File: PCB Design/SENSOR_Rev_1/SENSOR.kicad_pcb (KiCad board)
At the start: 2 copper layers, 40 x 65 mm, 17 parts, among them J1 Conn_01x24_Pin, J2 Conn_01x24_Pin, U1 MS583730BA01-50, U2 LIS2HH12TR, U3 MMC5603NJ, U4 LSM6DSO32TR

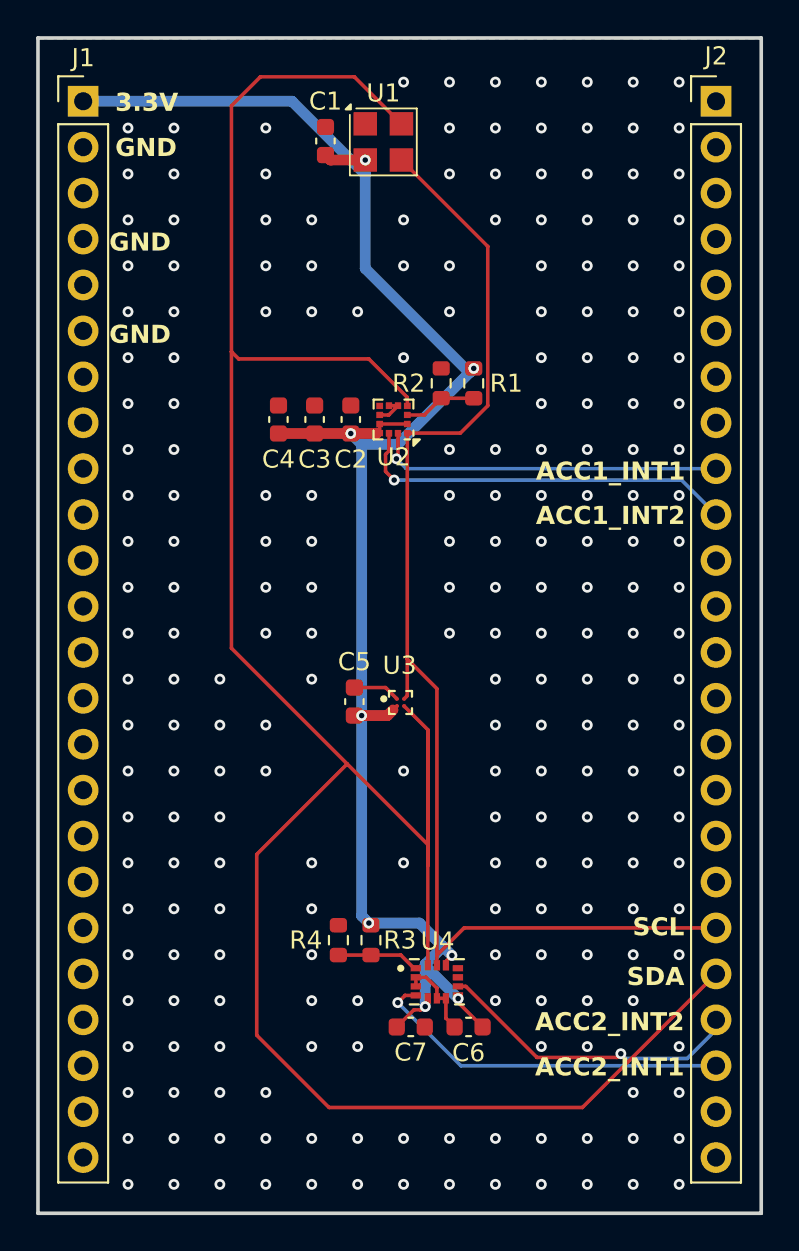
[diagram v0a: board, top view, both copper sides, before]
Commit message: Added Sensor Names to Silkscreen
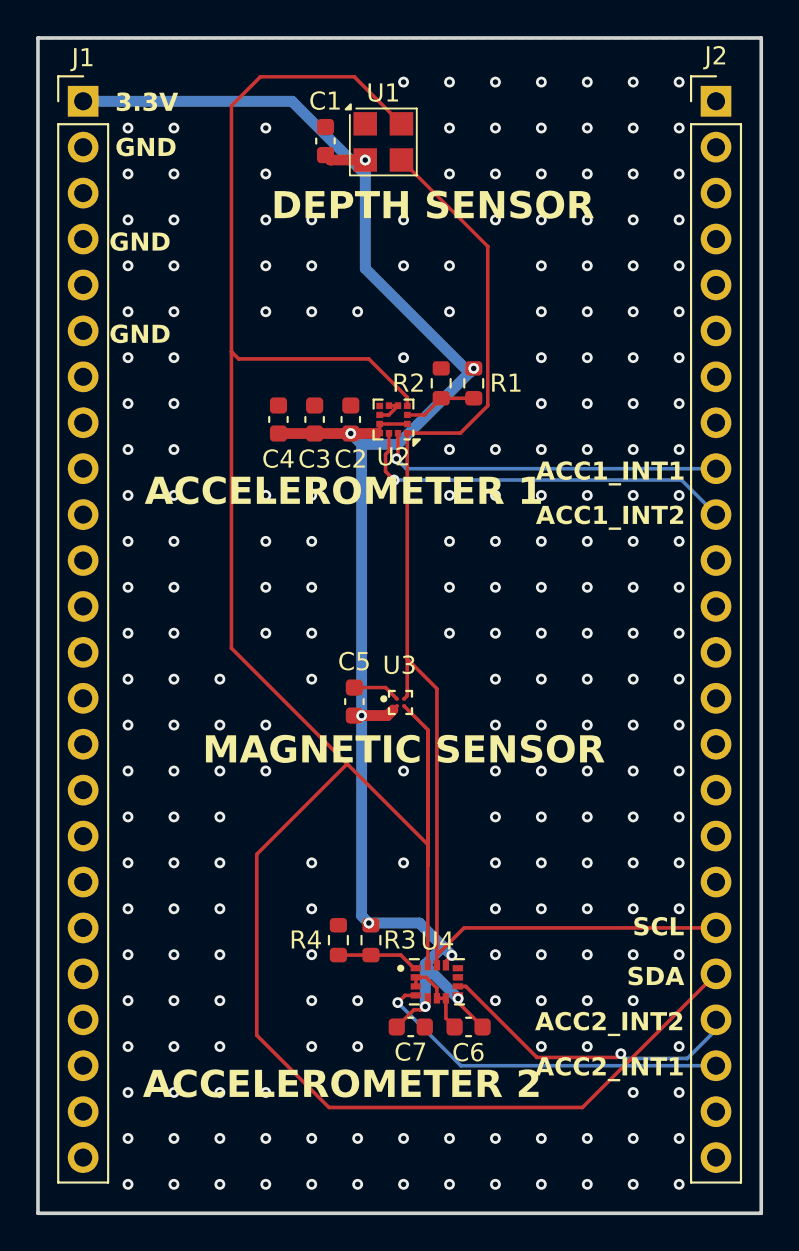
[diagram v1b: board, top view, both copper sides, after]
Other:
- board text added: "ACCELEROMETER 1"
- board text added: "ACCELEROMETER 2"
- board text added: "DEPTH SENSOR"
- board text added: "MAGNETIC SENSOR"
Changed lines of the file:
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@@
 			(drillshape 0)
 			(scaleselection 1)
-			(outputdirectory "SENSOR_BOARD_OUTPUT_08_18_2026/")
+			(outputdirectory "SENSOR_BOARD_OUTPUT_08_19_2026/")
 		)
 	)
@@
 		)
 	)
+	(gr_text "ACCELEROMETER 1"
+		(at 138.4 91.2 0)
+		(layer "F.SilkS")
+		(effects
+			(font
+				(size 1.5 1.5)
+				(thickness 0.3)
+				(bold yes)
+			)
+			(justify left bottom)
+		)
+	)
+	(gr_text "ACCELEROMETER 2"
+		(at 138.3 124 0)
+		(layer "F.SilkS")
+		(effects
+			(font
+				(size 1.5 1.5)
+				(thickness 0.3)
+				(bold yes)
+			)
+			(justify left bottom)
+		)
+	)
 	(gr_text "3.3V"
 		(at 136.76881 69.4 0)
@@
 		)
 	)
+	(gr_text "DEPTH SENSOR"
+		(at 145.4 75.4 0)
+		(layer "F.SilkS")
+		(effects
+			(font
+				(size 1.5 1.5)
+				(thickness 0.3)
+				(bold yes)
+			)
+			(justify left bottom)
+		)
+	)
 	(gr_text "SCL"
 		(at 168.25 115 0)
@@
 		)
 	)
+	(gr_text "MAGNETIC SENSOR"
+		(at 141.6 105.5 0)
+		(layer "F.SilkS")
+		(effects
+			(font
+				(size 1.5 1.5)
+				(thickness 0.3)
+				(bold yes)
+			)
+			(justify left bottom)
+		)
+	)

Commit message: Updated Sensor to new Version
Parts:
- U2: value LIS2HH12TR -> ASM330LHHXG1TR; footprint Package_LGA:LGA-12_2x2mm_P0.5mm -> SENSOR:LGA14_2P5X3_STM
- moved C3 2.60 mm to (149.1, 88.6), turned to 180 degrees
- moved C4 2.40 mm to (148.2, 86.2), turned to -90 degrees
- moved U2 0.29 mm to (152.3, 86.6), turned to -90 degrees
- moved C2 0.15 mm to (149.8, 86.2), turned to -90 degrees
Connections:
- U2 pad 1: /SCL -> /ACC1_ADD
- U2 pad 10: 3.3V -> unconnected-(U2-NC-Pad10)
- U2 pad 11: /ACC1_INT2 -> unconnected-(U2-NC-Pad11)
- U2 pad 12: /ACC1_INT1 -> 3.3V
- U2 pad 3: /ACC1_ADD -> 3.3V
- U2 pad 4: /SDA -> /ACC1_INT1
- U2 pad 5: GND -> 3.3V
- U2 pad 6: GND -> unconnected-(U2-NC-Pad6)
- U2 pad 8: GND -> 3.3V
- U2 pad 9: 3.3V -> /ACC1_INT2
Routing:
- net 3.3V: track 97.6 -> 105.3 mm, vias 8 -> 9
- net /ACC1_INT1: track 19.4 -> 21.2 mm
- net /SDA: track 138.4 -> 140.3 mm, vias 0 -> 2
- net /SCL: track 69.1 -> 70.8 mm
- net GND: track 9.07 -> 10.6 mm, vias 229 -> 232
- net /ACC1_INT2: track 21.5 -> 20.0 mm

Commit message: Claude PCB Review
Made updates based on Claude's Review
- Added decoupling capacitor
- Verified CS pins
- Compared placement and connections to data sheets
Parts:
- added C8: 10u, Capacitor_SMD:C_0603_1608Metric, F.Cu at (153.1, 121.5)
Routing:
- net 3.3V: track 105.3 -> 106.9 mm
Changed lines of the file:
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@@
 			(net 32 "/ACC1_ADD")
 			(pinfunction "SDO/SA0")
-			(pintype "unspecified")
+			(pintype "passive")
 		)
 		(pad "2" smd rect
@@
 			(net 1 "3.3V")
 			(pinfunction "MSDA")
-			(pintype "unspecified")
+			(pintype "passive")
 		)
 		(pad "3" smd rect
@@
 			(net 1 "3.3V")
 			(pinfunction "MSCL")
-			(pintype "unspecified")
+			(pintype "passive")
 		)
 		(pad "4" smd rect
@@
 			(net 35 "/ACC1_INT1")
 			(pinfunction "INT1")
-			(pintype "unspecified")
+			(pintype "passive")
 		)
 		(pad "5" smd rect
@@
 			(net 34 "/ACC1_INT2")
 			(pinfunction "INT2")
-			(pintype "unspecified")
+			(pintype "passive")
 		)
 		(pad "10" smd rect
@@
 			(net 1 "3.3V")
 			(pinfunction "CS")
-			(pintype "unspecified")
+			(pintype "passive")
 		)
 		(pad "13" smd rect
@@
 			(net 3 "/SCL")
 			(pinfunction "SCL")
-			(pintype "unspecified")
+			(pintype "passive")
 		)
 		(pad "14" smd rect
@@
 			(net 2 "/SDA")
 			(pinfunction "SDA")
-			(pintype "unspecified")
+			(pintype "passive")
 		)
 		(embedded_fonts no)
@@
 		(tags "capacitor")
 		(property "Reference" "C7"
-			(at 0 1.4 0)
+			(at -2.515 0.055 0)
 			(layer "F.SilkS")
 			(effects
@@
 		)
 	)
+	(footprint "Capacitor_SMD:C_0603_1608Metric"
+		(layer "F.Cu")
+		(at 153.125 121.5)
+		(descr "Capacitor SMD 0603 (1608 Metric), square (rectangular) end terminal, IPC-7351 nominal, (Body size source: IPC-SM-782 page 76, https://www.pcb-3d.com/wordpress/wp-content/uploads/ipc-sm-782a_amendment_1_and_2.pdf), generated with kicad-footprint-generator")
+		(tags "capacitor")
+		(property "Reference" "C8"
+			(at -2.425 0.1 0)
+			(layer "F.SilkS")
+			(effects
+				(font
+					(size 1 1)
+					(thickness 0.15)
+				)
+			)
+		)
+		(property "Value" "10u"
+			(at 0 1.43 0)
+			(layer "F.Fab")
+			(effects
+				(font
+					(size 1 1)
+					(thickness 0.15)
+				)
+			)
+		)
+		(property "Datasheet" "~"
+			(at 0 0 0)
+			(layer "F.Fab")
+			(hide yes)
+			(effects
+				(font
+					(size 1.27 1.27)
+					(thickness 0.15)
+				)
+			)
+		)
+		(property "Description" "Unpolarized capacitor"
+			(at 0 0 0)
+			(layer "F.Fab")
+			(hide yes)
+			(effects
+				(font
+					(size 1.27 1.27)
+					(thickness 0.15)
+				)
+			)
+		)
+		(property ki_fp_filters "C_*")
+		(sheetname "/")
+		(sheetfile "SENSOR.kicad_sch")
+		(attr smd)
+		(fp_line
+			(start -0.14058 -0.51)
+			(end 0.14058 -0.51)
+			(stroke
+				(width 0.12)
+				(type solid)
+			)
+			(layer "F.SilkS")
+		)
+		(fp_line
+			(start -0.14058 0.51)
+			(end 0.14058 0.51)
+			(stroke
+				(width 0.12)
+				(type solid)
+			)
+			(layer "F.SilkS")
+		)
+		(fp_line
+			(start -1.48 -0.73)
+			(end 1.48 -0.73)
+			(stroke
+				(width 0.05)
+				(type solid)
+			)
+			(layer "F.CrtYd")
+		)
+		(fp_line
+			(start -1.48 0.73)
+			(end -1.48 -0.73)
+			(stroke
+				(width 0.05)
+				(type solid)
+			)
+			(layer "F.CrtYd")
+		)
+		(fp_line
+			(start 1.48 -0.73)
+			(end 1.48 0.73)
+			(stroke
+				(width 0.05)
+				(type solid)
+			)
+			(layer "F.CrtYd")
+		)
+		(fp_line
+			(start 1.48 0.73)
+			(end -1.48 0.73)
+			(stroke
+				(width 0.05)
+				(type solid)
+			)
+			(layer "F.CrtYd")
+		)
+		(fp_line
+			(start -0.8 -0.4)
+			(end 0.8 -0.4)
+			(stroke
+				(width 0.1)
+				(type solid)
+			)
+			(layer "F.Fab")
+		)
+		(fp_line
+			(start -0.8 0.4)
+			(end -0.8 -0.4)
+			(stroke
+				(width 0.1)
+				(type solid)
+			)
+			(layer "F.Fab")
+		)
+		(fp_line
+			(start 0.8 -0.4)
+			(end 0.8 0.4)
+			(stroke
+				(width 0.1)
+				(type solid)
+			)
+			(layer "F.Fab")
+		)
+		(fp_line
+			(start 0.8 0.4)
+			(end -0.8 0.4)
+			(stroke
+				(width 0.1)
+				(type solid)
+			)
+			(layer "F.Fab")
+		)
+		(fp_text user "${REFERENCE}"
+			(at 0 0 0)
+			(layer "F.Fab")
+			(effects
+				(font
+					(size 0.4 0.4)
+					(thickness 0.06)
+				)
+			)
+		)
+		(pad "1" smd roundrect
+			(at -0.775 0)
+			(size 0.9 0.95)
+			(layers "F.Cu" "F.Mask" "F.Paste")
+			(roundrect_rratio 0.25)
+			(net 1 "3.3V")
+			(pintype "passive")
+		)
+		(pad "2" smd roundrect
+			(at 0.775 0)
+			(size 0.9 0.95)
+			(layers "F.Cu" "F.Mask" "F.Paste")
+			(roundrect_rratio 0.25)
+			(net 4 "GND")
+			(pintype "passive")
+		)
+		(embedded_fonts no)
+		(model "${KICAD9_3DMODEL_DIR}/Capacitor_SMD.3dshapes/C_0603_1608Metric.step"
+			(offset
+				(xyz 0 0 0)
+			)
+			(scale
+				(xyz 1 1 1)
+			)
+			(rotate
+				(xyz 0 0 0)
+			)
+		)
+	)
 	(footprint "SENSOR:XDCR_LSM6DSO32TR"
 		(layer "F.Cu")
@@
 	)
 	(gr_text "ACCELEROMETER 2"
-		(at 138.3 124 0)
+		(at 138.5 124.2 0)
 		(layer "F.SilkS")
 		(effects
@@
 	)
 	(segment
+		(start 152.35 121.5)
+		(end 152.35 119.955)
+		(width 0.6)
+		(layer "F.Cu")
+		(net 1)
+	)
+	(segment
 		(start 154.0625 118.673722)
 		(end 153.917005 118.819217)
@@
 		(layer "F.Cu")
 		(net 1)
+	)
+	(segment
+		(start 152.35 119.955)
+		(end 152.34 119.945)
+		(width 0.6)
+		(layer "F.Cu")
+		(net 1)

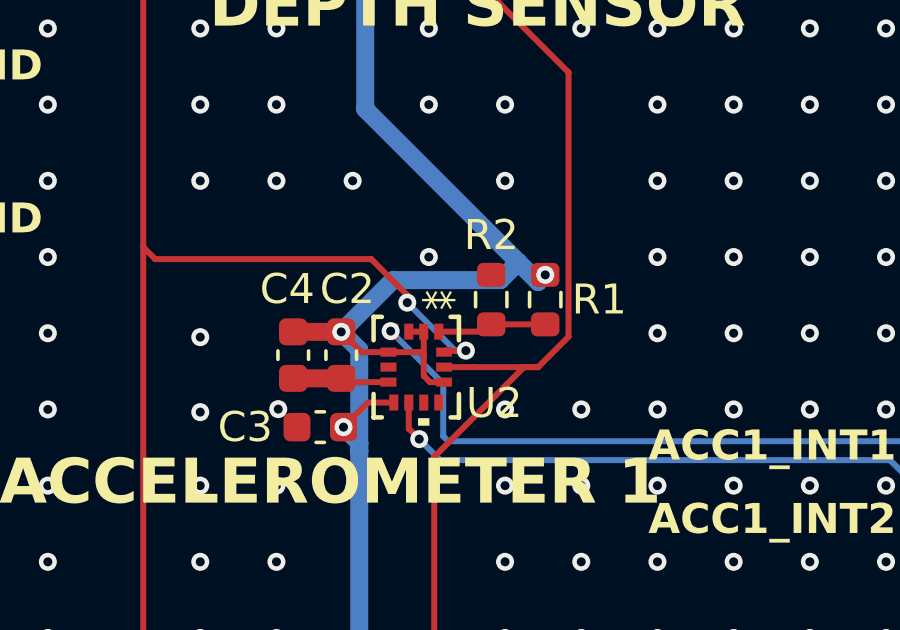
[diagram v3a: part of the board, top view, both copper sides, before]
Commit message: Claude Design Review
fix: tie ASM330 MSCL/MSDA to GND; DNP mark address jumpers R1/R3
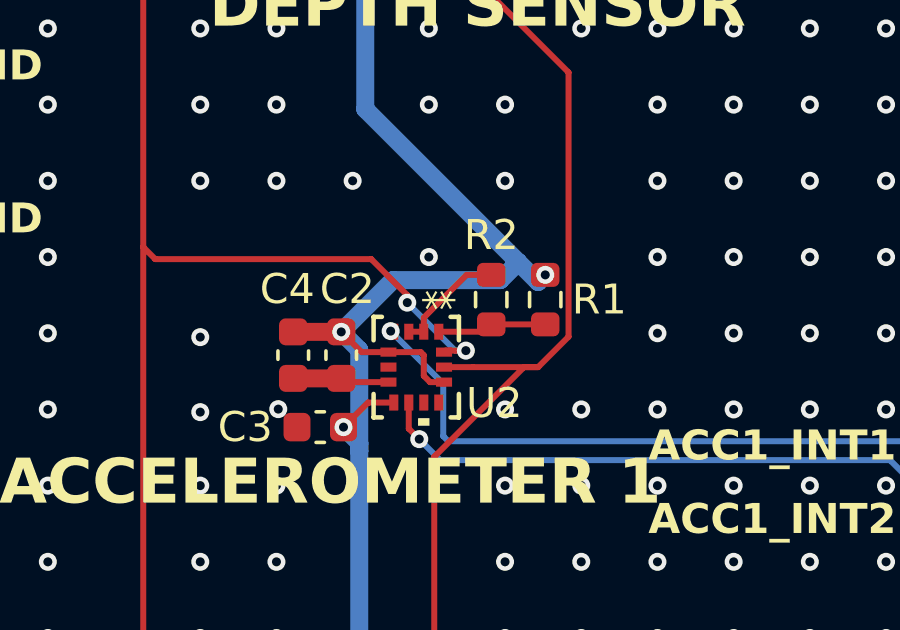
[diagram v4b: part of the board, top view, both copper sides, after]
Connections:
- J1 pad 3: 12V -> unconnected-(J1-Pin_3-Pad3)
- J1 pad 5: V_Piezo -> unconnected-(J1-Pin_5-Pad5)
- U2 pad 2: 3.3V -> GND
- U2 pad 3: 3.3V -> GND
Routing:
- net GND: track 10.6 -> 14.4 mm
- net 3.3V: track 106.9 -> 105.6 mm
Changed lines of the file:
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@@
 	(net 3 "/SCL")
 	(net 4 "GND")
-	(net 5 "12V")
-	(net 6 "V_Piezo")
+	(net 5 "unconnected-(J1-Pin_3-Pad3)")
+	(net 6 "unconnected-(J1-Pin_5-Pad5)")
 	(net 7 "unconnected-(J1-Pin_8-Pad8)")
 	(net 8 "unconnected-(J1-Pin_19-Pad19)")
@@
 			(size 0.3048 0.5334)
 			(layers "F.Cu" "F.Mask" "F.Paste")
-			(net 1 "3.3V")
+			(net 4 "GND")
 			(pinfunction "MSDA")
 			(pintype "passive")
@@
 			(size 0.3048 0.5334)
 			(layers "F.Cu" "F.Mask" "F.Paste")
-			(net 1 "3.3V")
+			(net 4 "GND")
 			(pinfunction "MSCL")
 			(pintype "passive")
@@
 		(sheetname "/")
 		(sheetfile "SENSOR.kicad_sch")
-		(attr smd)
+		(attr smd dnp)
 		(fp_line
 			(start -0.237258 -0.5225)
@@
 		(sheetname "/")
 		(sheetfile "SENSOR.kicad_sch")
-		(attr smd)
+		(attr smd dnp)
 		(fp_line
 			(start -0.237258 -0.5225)
@@
 			(layers "*.Cu" "*.Mask")
 			(remove_unused_layers no)
-			(net 5 "12V")
+			(net 5 "unconnected-(J1-Pin_3-Pad3)")
 			(pinfunction "Pin_3")
-			(pintype "passive")
+			(pintype "passive+no_connect")
 		)
 		(pad "4" thru_hole circle
@@
 			(layers "*.Cu" "*.Mask")
 			(remove_unused_layers no)
-			(net 6 "V_Piezo")
+			(net 6 "unconnected-(J1-Pin_5-Pad5)")
 			(pinfunction "Pin_5")
-			(pintype "passive")
+			(pintype "passive+no_connect")
 		)
 		(pad "6" thru_hole circle
@@
 	)
 	(segment
-		(start 152.550063 85.4189)
-		(end 152.049937 85.4189)
-		(width 0.2)
-		(layer "F.Cu")
-		(net 1)
-	)
-	(segment
 		(start 153.285 119)
 		(end 153.6645 119)
@@
 	)
 	(segment
-		(start 152.550063 86.2)
-		(end 152.550063 85.4189)
-		(width 0.2)
-		(layer "F.Cu")
-		(net 1)
-	)
-	(segment
 		(start 152.35 119.955)
 		(end 152.34 119.945)
@@
 	)
 	(segment
+		(start 152.550063 85.4189)
+		(end 152.550063 84.9522)
+		(width 0.2)
+		(layer "F.Cu")
+		(net 4)
+	)
+	(segment
+		(start 153.977263 83.525)
+		(end 154.8 83.525)
+		(width 0.2)
+		(layer "F.Cu")
+		(net 4)
+	)
+	(segment
 		(start 155.0625 118.3625)
 		(end 155.0625 119.4675)
@@
 	)
 	(segment
+		(start 152.049937 85.4189)
+		(end 152.550063 85.4189)
+		(width 0.2)
+		(layer "F.Cu")
+		(net 4)
+	)
+	(segment
 		(start 153.9645 117.2)
 		(end 153.4 117.2)
@@
 		(width 0.2)
 		(layer "F.Cu")
+		(net 4)
+	)
+	(segment
+		(start 152.550063 84.9522)
+		(end 153.977263 83.525)
+		(width 0.2)
+		(layer "F.Cu")

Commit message: Added Sensor Board Exports
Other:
- board text added: "SENSOR BOARD REV1.1 03/2026 By Samantha Chong"
- board text removed: "SENSOR BOARD REV1 03/2026 By Samantha Chong"
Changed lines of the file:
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@@
 			(drillshape 0)
 			(scaleselection 1)
-			(outputdirectory "SENSOR_BOARD_OUTPUT_08_19_2026/")
+			(outputdirectory "SENSOR_BOARD_OUTPUT_08_22_2026/")
 		)
 	)
@@
 		)
 	)
-	(gr_text "SENSOR BOARD \nREV1 03/2026\nBy Samantha Chong"
+	(gr_text "SENSOR BOARD \nREV1.1 03/2026\nBy Samantha Chong"
 		(at 158.25 128.5 0)
 		(layer "B.SilkS")

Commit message: SENSOR - Added and Exported 3D Model of PCB
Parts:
- U1: footprint Sensor_Pressure:TE_MS5837-xxBA -> SENSOR:TE_MS5837-xxBA
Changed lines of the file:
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@@
 		)
 	)
-	(footprint "Sensor_Pressure:TE_MS5837-xxBA"
+	(footprint "SENSOR:TE_MS5837-xxBA"
 		(layer "F.Cu")
 		(at 151.6 71)
@@
 		)
 		(embedded_fonts no)
-		(model "${KICAD9_3DMODEL_DIR}/Sensor_Pressure.3dshapes/TE_MS5837-xxBA.step"
+		(model "${KIPRJMOD}/Library/MS583730BA01-50--3DModel-STEP-510211.STEP"
 			(offset
 				(xyz 0 0 0)
@@
 			)
 			(rotate
-				(xyz 0 0 0)
-			)
-		)
+				(xyz -90 -0 -0)
+			)
+		)
